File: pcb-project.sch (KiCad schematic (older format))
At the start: 154 parts, among them SW1 SW_PUSH, U2 ATMEGA32U4, X2 XTAL_GND

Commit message: RGB Tracing Completed
Ready for production files to be created and sent off to JLCPCB.
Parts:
- added D_RGB8: WS2812B, LED_SMD:LED_WS2812B_PLCC4_5.0x5.0mm_P3.2mm, symbol LED:WS2812B
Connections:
- net +5V: now also D_RGB8.1 (VDD)
- net GND: now also D_RGB8.3 (VSS)
- net at D_RGB7.2 (DOUT): now also D_RGB8.4 (DIN)
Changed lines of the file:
@@
 Connection ~ 17500 6600
-Wire Wire Line
-	17500 6600 17775 6600
 Wire Wire Line
 	12750 5750 12750 6000
 $Comp
-L power:+5V #PWR?
+L power:+5V #PWR0114
 U 1 1 5CE35697
 P 12750 5750
-F 0 "#PWR?" H 12750 5600 50  0001 C CNN
+F 0 "#PWR0114" H 12750 5600 50  0001 C CNN
 F 1 "+5V" H 12765 5923 50  0000 C CNN
 F 2 "" H 12750 5750 50  0001 C CNN
@@
 $EndComp
 Wire Wire Line
-	17775 6600 17775 6850
+	18550 6600 18550 6850
 $Comp
-L power:GND #PWR?
+L power:GND #PWR0115
 U 1 1 5CEBC71F
-P 17775 6850
-F 0 "#PWR?" H 17775 6600 50  0001 C CNN
-F 1 "GND" H 17780 6677 50  0000 C CNN
-F 2 "" H 17775 6850 50  0001 C CNN
-F 3 "" H 17775 6850 50  0001 C CNN
-	1    17775 6850
+P 18550 6850
+F 0 "#PWR0115" H 18550 6600 50  0001 C CNN
+F 1 "GND" H 18555 6677 50  0000 C CNN
+F 2 "" H 18550 6850 50  0001 C CNN
+F 3 "" H 18550 6850 50  0001 C CNN
+	1    18550 6850
 	1    0    0    -1
 $EndComp
@@
 Wire Wire Line
 	12550 6300 12700 6300
+$Comp
+L LED:WS2812B D_RGB8
+U 1 1 5D081DEA
+P 18250 6300
+F 0 "D_RGB8" H 18594 6346 50  0000 L CNN
+F 1 "WS2812B" H 18594 6255 50  0000 L CNN
+F 2 "LED_SMD:LED_WS2812B_PLCC4_5.0x5.0mm_P3.2mm" H 18300 6000 50  0001 L TNN
+F 3 "https://cdn-shop.adafruit.com/datasheets/WS2812B.pdf" H 18350 5925 50  0001 L TNN
+	1    18250 6300
+	1    0    0    -1
+$EndComp
+Wire Wire Line
+	17800 6300 17950 6300
+Wire Wire Line
+	17500 6000 18250 6000
+Connection ~ 17500 6000
+Connection ~ 18250 6600
+Wire Wire Line
+	18250 6600 18550 6600
+Wire Wire Line
+	17500 6600 18250 6600
 $EndSCHEMATC

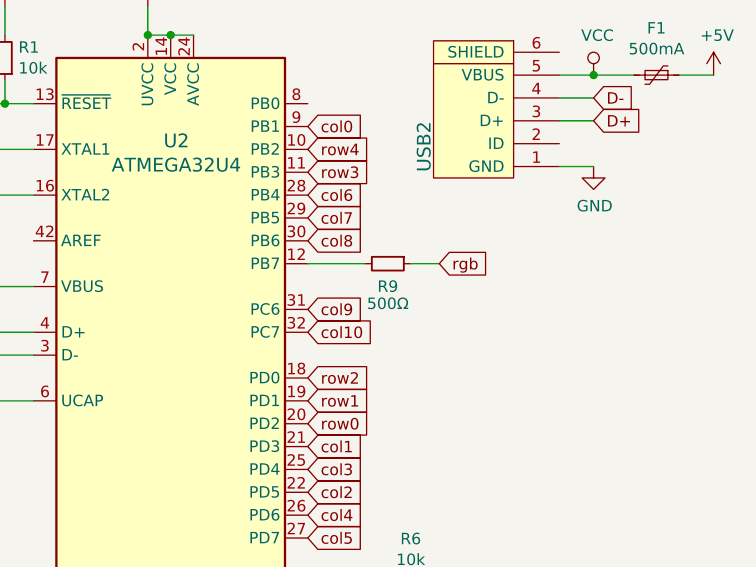
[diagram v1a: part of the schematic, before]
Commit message: Removed Unnecessary Resistor on RGB Data Trace
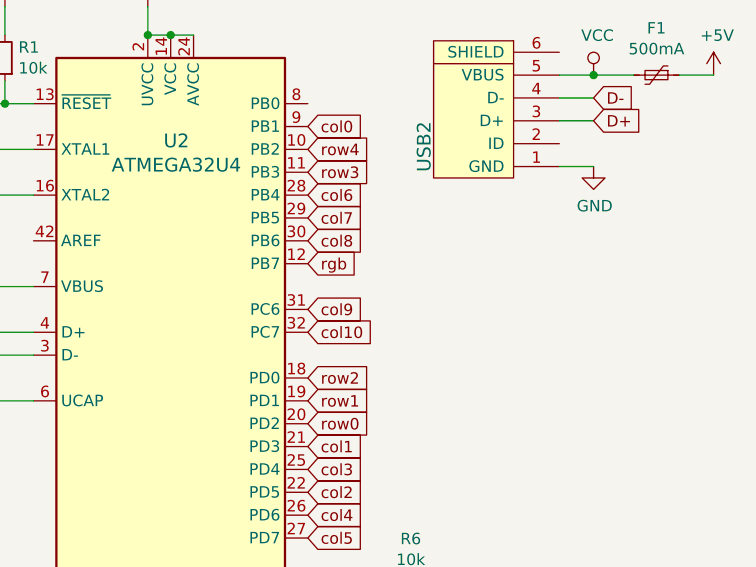
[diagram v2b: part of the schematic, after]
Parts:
- removed R9: 500Ω, Resistor_SMD:R_0805_2012Metric, symbol Device:R_Small
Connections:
- net rgb: now also U2.12 (PB7)
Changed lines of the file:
@@
 Wire Wire Line
 	17200 6300 17050 6300
-$Comp
-L Device:R_Small R9
-U 1 1 5CFACD8B
-P 20775 3750
-F 0 "R9" V 20875 3750 50  0000 C CNN
-F 1 "500Ω" V 20950 3750 50  0000 C CNN
-F 2 "Resistor_SMD:R_0805_2012Metric" H 20775 3750 50  0001 C CNN
-F 3 "~" H 20775 3750 50  0001 C CNN
-	1    20775 3750
-	0    1    1    0
-$EndComp
-Wire Wire Line
-	20425 3750 20675 3750
-Text GLabel 21000 3750 2    50   Input ~ 0
+Text GLabel 20425 3750 2    50   Input ~ 0
 rgb
-Wire Wire Line
-	20875 3750 21000 3750
 Text GLabel 12550 6300 0    50   Input ~ 0
 rgb
